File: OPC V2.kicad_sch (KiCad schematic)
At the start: 17 parts, among them J1 691382010004, J2 691382010004, J3 691382010004

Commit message: maj puissance
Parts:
- R2: value 3k3 -> 16k5
- R3, R4: value 16k5 -> 1M; LCSC Part # (none) -> C23182
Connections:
- net +3V3: now also R3.2
- net AINN: now also U1.4 (COM2), U2.4 (COM2), U3.4 (COM2), U5.11 (NO4); no longer U1.2 (COM1), U2.2 (COM1), U3.2 (COM1)
- net AINP: now also U5.8 (NO3)
- net GND: no longer R3.2
- net VREF: now also U1.2 (COM1), U2.2 (COM1), U3.2 (COM1); no longer U1.4 (COM2), U2.4 (COM2), U3.4 (COM2), U5.11 (NO4), U5.8 (NO3)
- net 16k5_1 renamed TC_VCC
- net 16k5_2 renamed TC_GND
- net 3k3_1 renamed 3k3
- net 3k3_2 renamed 16k5
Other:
- note added: "Multiplexeur pour adapter les types de mesures (pt100 // pt1000 // TC)"
- note removed: "Multiplexeur pour adapter le courant de mesure (pt100 // pt1000)"
- moved on the sheet: R1

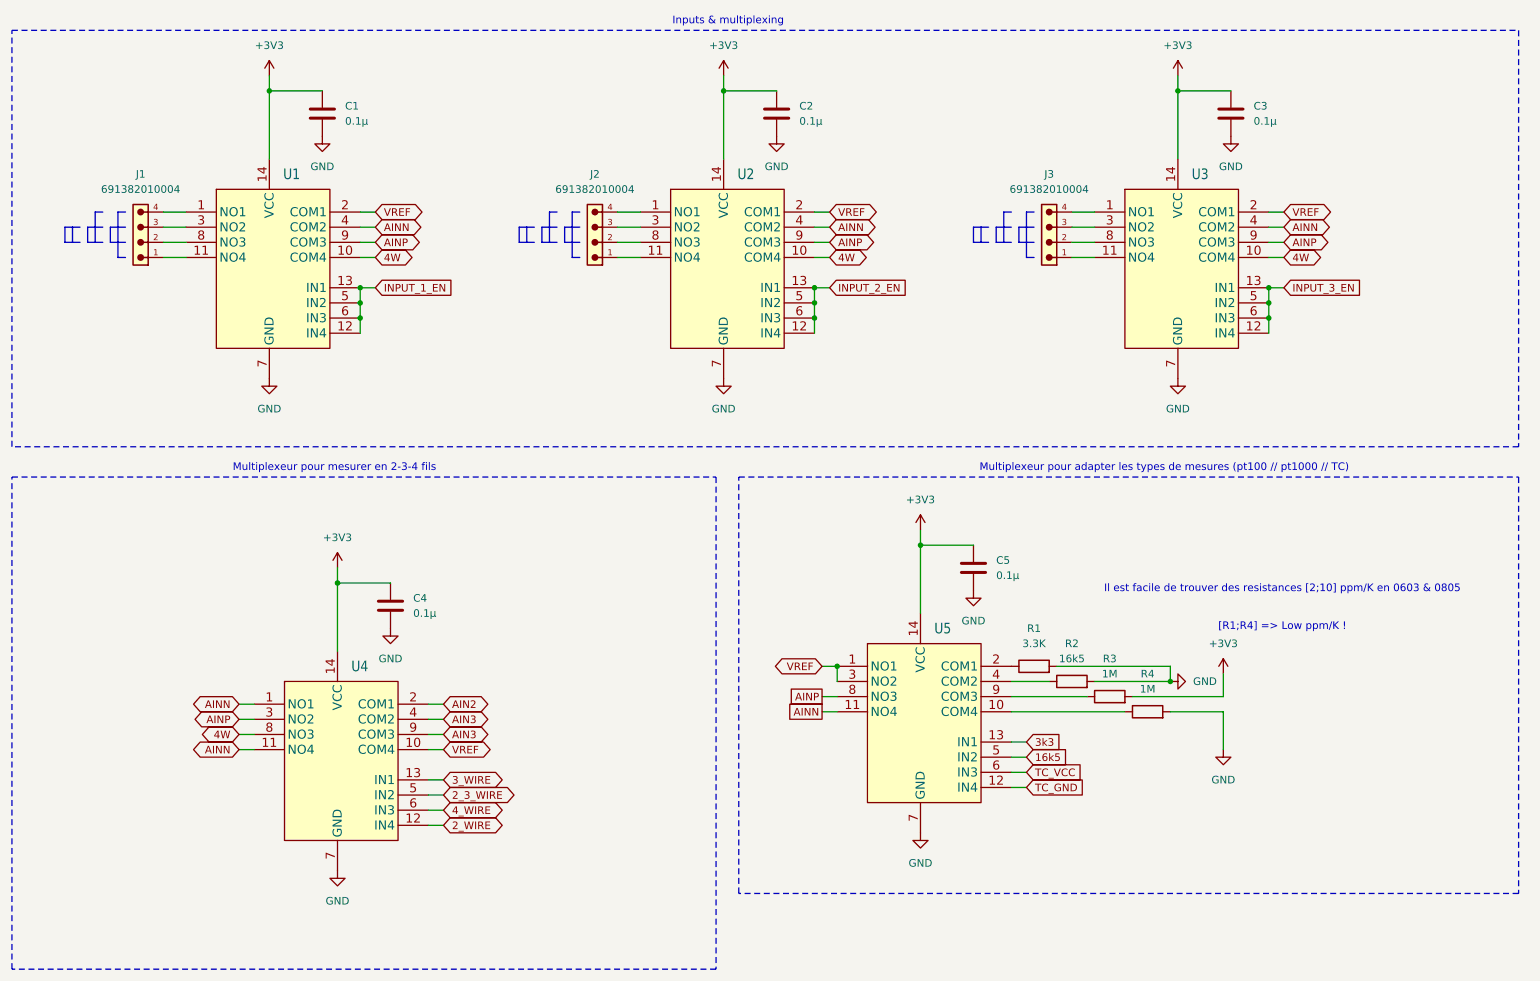
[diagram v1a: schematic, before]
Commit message: découpage et hierarchie
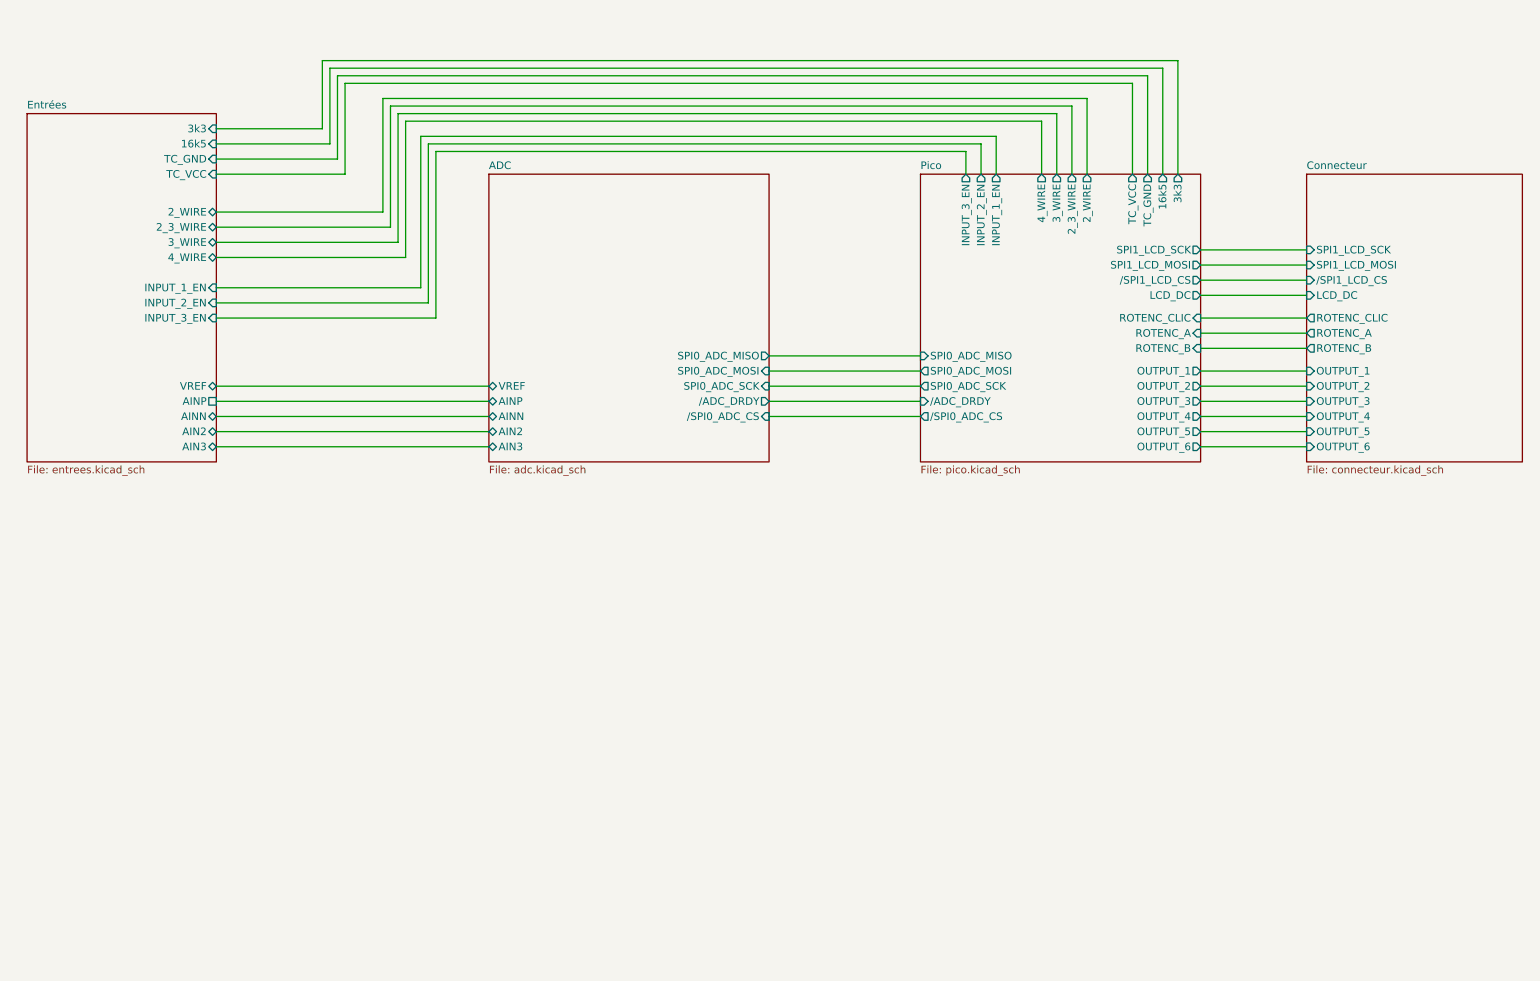
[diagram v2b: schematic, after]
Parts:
- removed C1, C2, C3, C4, C5: 0.1µ, Capacitor_SMD:C_0603_1608Metric_Pad1.08x0.95mm_HandSolder, symbol Device:C
- removed J1, J2, J3: 691382010004, OPC:691382010004, symbol OPC:691382010004
- removed R1: 3.3K, Resistor_SMD:R_0603_1608Metric_Pad0.98x0.95mm_HandSolder, symbol Device:R
- removed R2: 16k5, Resistor_SMD:R_0603_1608Metric_Pad0.98x0.95mm_HandSolder, symbol Device:R
- removed R3, R4: 1M, Resistor_SMD:R_0603_1608Metric_Pad0.98x0.95mm_HandSolder, symbol Device:R
- removed U1, U2, U3, U4, U5: (no value), OPC:TSSOP-14_4.4x5mm_P0.65mm, symbol OPC:TS3A4751PWR
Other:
- added sheet ADC (adc.kicad_sch)
- added sheet Connecteur (connecteur.kicad_sch)
- added sheet Entrées (entrees.kicad_sch)
- added sheet Pico (pico.kicad_sch)
- note removed: "Il est facile de trouver des resistances [2;10] ppm/K en 0603 & 0805"
- note removed: "Inputs & multiplexing"
- note removed: "Multiplexeur pour adapter les types de mesures (pt100 // pt1000 // TC)"
- note removed: "Multiplexeur pour mesurer en 2-3-4 fils"
- note removed: "[R1;R4] => Low ppm/K !"

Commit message: corrections
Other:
- sheet Entrées ports: added RREF_16k5, RREF_1k65; removed 16k5, 3k3
- sheet Pico ports: added RREF_16k5, RREF_1k65; removed 16k5, 3k3
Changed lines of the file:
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@@
-			)
-		)
-		(pin "3k3" output
-			(at 218.44 41.91 90)
-			(effects
-				(font
-					(size 1.27 1.27)
-				)
-				(justify right)
 			)
 		)
@@
 			)
 		)
-		(pin "16k5" output
-			(at 215.9 41.91 90)
-			(effects
-				(font
-					(size 1.27 1.27)
-				)
-				(justify right)
-			)
-		)
 		(pin "INPUT_1_EN" output
 			(at 187.96 41.91 90)
@@
 		(pin "{slash}SPI1_LCD_CS" output
 			(at 222.25 59.69 0)
+			(effects
+				(font
+					(size 1.27 1.27)
+				)
+				(justify right)
+			)
+		)
+		(pin "RREF_1k65" output
+			(at 215.9 41.91 90)
+			(effects
+				(font
+					(size 1.27 1.27)
+				)
+				(justify right)
+			)
+		)
+		(pin "RREF_16k5" output
+			(at 218.44 41.91 90)
 			(effects
 				(font
@@
 			)
 		)
-		(pin "3k3" input
-			(at 57.15 34.29 0)
-			(effects
-				(font
-					(size 1.27 1.27)
-				)
-				(justify right)
-			)
-		)
 		(pin "3_WIRE" bidirectional
 			(at 57.15 53.34 0)
@@
 			)
 		)
-		(pin "16k5" input
-			(at 57.15 36.83 0)
-			(effects
-				(font
-					(size 1.27 1.27)
-				)
-				(justify right)
-			)
-		)
 		(pin "AIN2" bidirectional
 			(at 57.15 85.09 0)
@@
 			)
 		)
-		(pin "AINP" passive
+		(pin "AINP" bidirectional
 			(at 57.15 80.01 0)
 			(effects
@@
 			(effects
 				(font
+					(size 1.27 1.27)
+				)
+				(justify right)
+			)
+		)
+		(pin "RREF_1k65" input
+			(at 57.15 34.29 0)
+			(effects
+				(font
+					(size 1.27 1.27)
+				)
+				(justify right)
+			)
+		)
+		(pin "RREF_16k5" input
+			(at 57.15 36.83 0)
+			(effects
+				(font

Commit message: daily
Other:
- title: Entrées & multiplexage -> Carte capteur + microcontroleur
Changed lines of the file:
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@@
 	(paper "A4")
 	(title_block
-		(title "Entrées & multiplexage")
+		(title "Carte capteur + microcontroleur")
 		(date "2026-07-30")
 		(rev "2")
